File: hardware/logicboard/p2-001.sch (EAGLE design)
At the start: 65 parts, among them IC1 74LS06N, IC11 74LS153D, IC12 LTC485S, IC13 LTC485S, IC2 4066N, J1 MKR, J11 Qwiic, J12 Qwiic, J13 Qwiic, J14 Qwiic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

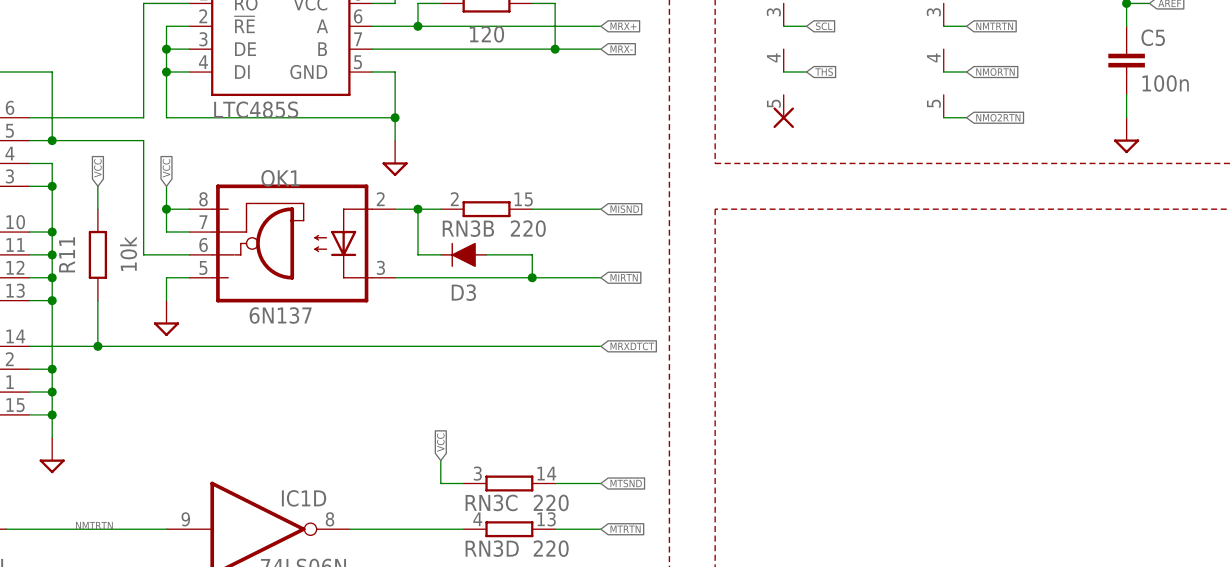
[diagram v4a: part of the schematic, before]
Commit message: TLP552 -> TLP2630.
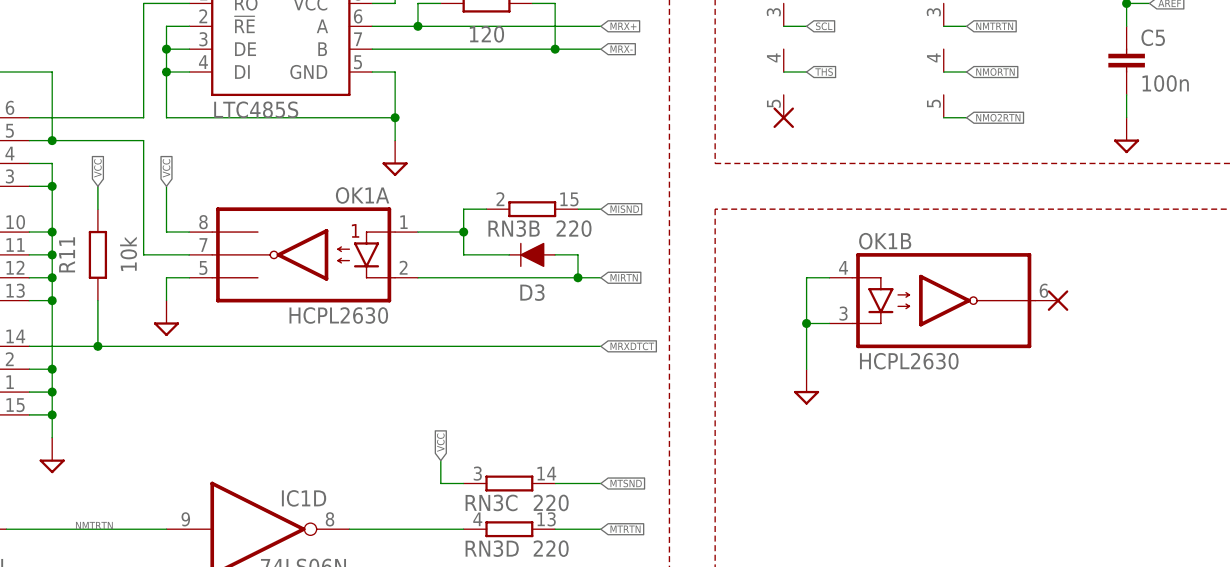
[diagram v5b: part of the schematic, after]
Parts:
- OK1: value 6N137 -> HCPL2630; device optocoupler:6N137 -> optocoupler:HCPL2630
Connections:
- net GND: now also OK1A.GND, OK1B.A2, OK1B.C2; no longer OK1.GND
- net MIDIINSND: now also OK1A.A1; no longer OK1.A
- net MIN: now also OK1A.VO1; no longer OK1.VO
- net MIRTN: now also OK1A.C1; no longer OK1.C
- net VCC: now also OK1A.VCC; no longer OK1.VCC, OK1.VE
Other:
- moved on the sheet: D3, RN3B
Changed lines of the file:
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@@
 <part name="MC1" library="adafruit" deviceset="ARDUINOMICRO" device=""/>
 <part name="SUPPLY18" library="supply2" deviceset="GND" device=""/>
-<part name="OK1" library="optocoupler" library_urn="urn:adsk.eagle:library:320" deviceset="6N137" device="" package3d_urn="urn:adsk.eagle:package:21941/1"/>
 <part name="D3" library="SparkFun-DiscreteSemi" library_urn="urn:adsk.eagle:library:514" deviceset="DIODE" device="-1N4148" package3d_urn="urn:adsk.eagle:package:38452/1" value=""/>
 <part name="LOGO1" library="SparkFun-Aesthetics" deviceset="OSHW-LOGO" device="S-COPPER" value="OSHW-LOGOS-COPPER"/>
@@
 <part name="RN4" library="resistor-net" library_urn="urn:adsk.eagle:library:343" deviceset="RN04" device="" package3d_urn="urn:adsk.eagle:package:24976/1" value="4.7k"/>
 <part name="X1" library="wirepad" library_urn="urn:adsk.eagle:library:412" deviceset="PAD-N" device=""/>
+<part name="OK1" library="optocoupler" library_urn="urn:adsk.eagle:library:320" deviceset="HCPL2630" device="" package3d_urn="urn:adsk.eagle:package:21941/1"/>
+<part name="SUPPLY1" library="supply2" deviceset="GND" device=""/>
+<part name="X2" library="wirepad" library_urn="urn:adsk.eagle:library:412" deviceset="PAD-N" device=""/>
 </parts>
 <sheets>
@@
 <instance part="MC1" gate="G$1" x="83.82" y="213.36" smashed="yes" rot="R270"/>
 <instance part="SUPPLY18" gate="GND" x="322.58" y="198.12" smashed="yes"/>
-<instance part="OK1" gate="A" x="177.8" y="119.38" smashed="yes" rot="MR0">
-<attribute name="NAME" x="177.8" y="127" size="1.778" layer="95" align="bottom-center"/>
-<attribute name="VALUE" x="177.8" y="111.76" size="1.778" layer="96" align="bottom-center"/>
-</instance>
-<instance part="D3" gate="G$1" x="198.12" y="119.38" smashed="yes" rot="R180">
-<attribute name="NAME" x="198.12" y="114.3" size="1.778" layer="95" align="bottom-center"/>
-<attribute name="VALUE" x="200.66" y="121.412" size="1.778" layer="96" font="vector" rot="R180" align="top-left"/>
+<instance part="D3" gate="G$1" x="205.74" y="119.38" smashed="yes" rot="R180">
+<attribute name="NAME" x="205.74" y="114.3" size="1.778" layer="95" align="bottom-center"/>
+<attribute name="VALUE" x="208.28" y="121.412" size="1.778" layer="96" font="vector" rot="R180" align="top-left"/>
 </instance>
 <instance part="LOGO1" gate="G$1" x="370.84" y="248.92" smashed="yes"/>
@@
 <attribute name="NAME" x="195.58" y="14.732" size="1.778" layer="95"/>
 </instance>
-<instance part="RN3" gate="B" x="200.66" y="124.46" smashed="yes">
-<attribute name="VALUE" x="203.2" y="121.412" size="1.778" layer="96"/>
-<attribute name="NAME" x="195.58" y="121.412" size="1.778" layer="95"/>
+<instance part="RN3" gate="B" x="205.74" y="124.46" smashed="yes">
+<attribute name="VALUE" x="208.28" y="121.412" size="1.778" layer="96"/>
+<attribute name="NAME" x="200.66" y="121.412" size="1.778" layer="95"/>
 </instance>
 <instance part="RN3" gate="C" x="203.2" y="93.98" smashed="yes">
@@
 </instance>
 <instance part="X1" gate="G$1" x="233.68" y="134.62" smashed="yes"/>
+<instance part="OK1" gate="A" x="180.34" y="119.38" smashed="yes" rot="MR0">
+<attribute name="NAME" x="189.865" y="125.095" size="1.778" layer="95" rot="MR0"/>
+<attribute name="VALUE" x="189.865" y="111.76" size="1.778" layer="96" rot="MR0"/>
+</instance>
+<instance part="OK1" gate="B" x="251.46" y="114.3" smashed="yes">
+<attribute name="NAME" x="241.935" y="120.015" size="1.778" layer="95"/>
+<attribute name="VALUE" x="241.935" y="106.68" size="1.778" layer="96"/>
+</instance>
+<instance part="SUPPLY1" gate="GND" x="236.22" y="104.14" smashed="yes"/>
+<instance part="X2" gate="G$1" x="264.16" y="114.3" smashed="yes"/>
 </instances>
 <busses>
@@
 </segment>
 <segment>
-<pinref part="OK1" gate="A" pin="GND"/>
 <pinref part="SUPPLY29" gate="GND" pin="GND"/>
 <wire x1="167.64" y1="116.84" x2="165.1" y2="116.84" width="0.1524" layer="91"/>
 <wire x1="165.1" y1="116.84" x2="165.1" y2="114.3" width="0.1524" layer="91"/>
+<pinref part="OK1" gate="A" pin="GND"/>
 </segment>
 <segment>
@@
 <label x="43.18" y="162.56" size="0.8128" layer="95" xref="yes"/>
 </segment>
+<segment>
+<pinref part="OK1" gate="B" pin="A2"/>
+<wire x1="238.76" y1="116.84" x2="236.22" y2="116.84" width="0.1524" layer="91"/>
+<pinref part="OK1" gate="B" pin="C2"/>
+<wire x1="238.76" y1="111.76" x2="236.22" y2="111.76" width="0.1524" layer="91"/>
+<wire x1="236.22" y1="111.76" x2="236.22" y2="116.84" width="0.1524" layer="91"/>
+<wire x1="236.22" y1="111.76" x2="236.22" y2="106.68" width="0.1524" layer="91"/>
+<junction x="236.22" y="111.76"/>
+<pinref part="SUPPLY1" gate="GND" pin="GND"/>
+</segment>
 </net>
 <net name="VCC" class="2">
@@
 </segment>
 <segment>
-<pinref part="OK1" gate="A" pin="VE"/>
 <wire x1="167.64" y1="121.92" x2="165.1" y2="121.92" width="0.1524" layer="91"/>
-<wire x1="165.1" y1="121.92" x2="165.1" y2="124.46" width="0.1524" layer="91"/>
+<wire x1="165.1" y1="121.92" x2="165.1" y2="127" width="0.1524" layer="91"/>
+<label x="165.1" y="127" size="0.8128" layer="95" rot="R90" xref="yes"/>
 <pinref part="OK1" gate="A" pin="VCC"/>
-<wire x1="165.1" y1="124.46" x2="165.1" y2="127" width="0.1524" layer="91"/>
-<wire x1="167.64" y1="124.46" x2="165.1" y2="124.46" width="0.1524" layer="91"/>
-<junction x="165.1" y="124.46"/>
-<label x="165.1" y="127" size="0.8128" layer="95" rot="R90" xref="yes"/>
 </segment>
 <segment>
@@
 <net name="MIDIINSND" class="0">
 <segment>
-<pinref part="OK1" gate="A" pin="A"/>
-<wire x1="193.04" y1="124.46" x2="190.5" y2="124.46" width="0.1524" layer="91"/>
-<wire x1="193.04" y1="124.46" x2="193.04" y2="119.38" width="0.1524" layer="91"/>
+<wire x1="198.12" y1="124.46" x2="198.12" y2="121.92" width="0.1524" layer="91"/>
 <pinref part="D3" gate="G$1" pin="C"/>
-<wire x1="193.04" y1="119.38" x2="195.58" y2="119.38" width="0.1524" layer="91"/>
-<wire x1="195.58" y1="124.46" x2="193.04" y2="124.46" width="0.1524" layer="91"/>
-<junction x="193.04" y="124.46"/>
+<wire x1="198.12" y1="121.92" x2="198.12" y2="119.38" width="0.1524" layer="91"/>
+<wire x1="198.12" y1="119.38" x2="203.2" y2="119.38" width="0.1524" layer="91"/>
+<wire x1="200.66" y1="124.46" x2="198.12" y2="124.46" width="0.1524" layer="91"/>
 <pinref part="RN3" gate="B" pin="1"/>
+<pinref part="OK1" gate="A" pin="A1"/>
+<wire x1="193.04" y1="121.92" x2="198.12" y2="121.92" width="0.1524" layer="91"/>
+<junction x="198.12" y="121.92"/>
 </segment>
 </net>
@@
 <segment>
 <pinref part="IC11" gate="A" pin="1C1"/>
-<pinref part="OK1" gate="A" pin="VO"/>
 <wire x1="149.86" y1="132.08" x2="152.4" y2="132.08" width="0.1524" layer="91"/>
 <wire x1="152.4" y1="132.08" x2="162.56" y2="132.08" width="0.1524" layer="91"/>
@@
 <wire x1="132.08" y1="144.78" x2="139.7" y2="144.78" width="0.1524" layer="91"/>
 <junction x="139.7" y="144.78"/>
+<pinref part="OK1" gate="A" pin="VO1"/>
 </segment>
 </net>
@@
 <net name="MISND" class="0">
 <segment>
-<wire x1="205.74" y1="124.46" x2="213.36" y2="124.46" width="0.1524" layer="91"/>
+<wire x1="210.82" y1="124.46" x2="213.36" y2="124.46" width="0.1524" layer="91"/>
 <label x="213.36" y="124.46" size="0.8128" layer="95" xref="yes"/>
 <pinref part="RN3" gate="B" pin="2"/>
@@
 <segment>
 <pinref part="D3" gate="G$1" pin="A"/>
-<wire x1="200.66" y1="119.38" x2="205.74" y2="119.38" width="0.1524" layer="91"/>
-<wire x1="205.74" y1="119.38" x2="205.74" y2="116.84" width="0.1524" layer="91"/>
-<pinref part="OK1" gate="A" pin="C"/>
-<wire x1="205.74" y1="116.84" x2="190.5" y2="116.84" width="0.1524" layer="91"/>
-<wire x1="205.74" y1="116.84" x2="213.36" y2="116.84" width="0.1524" layer="91"/>
-<junction x="205.74" y="116.84"/>
+<wire x1="208.28" y1="119.38" x2="210.82" y2="119.38" width="0.1524" layer="91"/>
+<wire x1="210.82" y1="119.38" x2="210.82" y2="116.84" width="0.1524" layer="91"/>
+<wire x1="210.82" y1="116.84" x2="193.04" y2="116.84" width="0.1524" layer="91"/>
+<wire x1="210.82" y1="116.84" x2="213.36" y2="116.84" width="0.1524" layer="91"/>
+<junction x="210.82" y="116.84"/>
 <label x="213.36" y="116.84" size="0.8128" layer="95" xref="yes"/>
-</segment>
-</net>
+<pinref part="OK1" gate="A" pin="C1"/>
+</segment>
+</net>

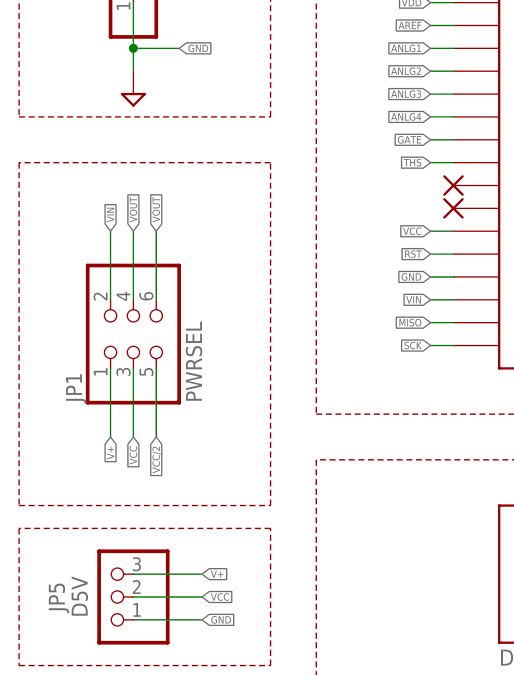
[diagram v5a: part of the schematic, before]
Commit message: Pads to close V+ and Vin.
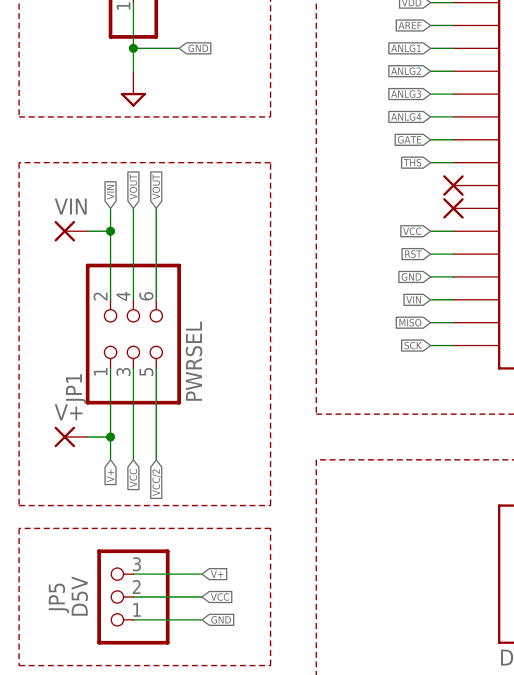
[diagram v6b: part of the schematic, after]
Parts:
- added V+, VIN: (no value), wirepad:SMD2
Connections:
- net V+: now also V+.P
- net VIN: now also VIN.P
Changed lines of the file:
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@@
 <part name="SUPPLY1" library="supply2" deviceset="GND" device=""/>
 <part name="X2" library="wirepad" library_urn="urn:adsk.eagle:library:412" deviceset="PAD-N" device=""/>
+<part name="V+" library="wirepad" library_urn="urn:adsk.eagle:library:412" deviceset="SMD2" device="" package3d_urn="urn:adsk.eagle:package:30839/1"/>
+<part name="VIN" library="wirepad" library_urn="urn:adsk.eagle:library:412" deviceset="SMD2" device="" package3d_urn="urn:adsk.eagle:package:30839/1"/>
 </parts>
 <sheets>
@@
 <instance part="SUPPLY1" gate="GND" x="236.22" y="104.14" smashed="yes"/>
 <instance part="X2" gate="G$1" x="264.16" y="114.3" smashed="yes"/>
+<instance part="V+" gate="1" x="27.94" y="182.88" smashed="yes">
+<attribute name="NAME" x="26.797" y="184.7342" size="1.778" layer="95"/>
+<attribute name="VALUE" x="26.797" y="179.578" size="1.778" layer="96"/>
+</instance>
+<instance part="VIN" gate="1" x="27.94" y="205.74" smashed="yes">
+<attribute name="NAME" x="26.797" y="207.5942" size="1.778" layer="95"/>
+<attribute name="VALUE" x="26.797" y="202.438" size="1.778" layer="96"/>
+</instance>
 </instances>
 <busses>
@@
 <segment>
 <pinref part="JP1" gate="A" pin="3"/>
-<wire x1="35.56" y1="190.5" x2="35.56" y2="182.88" width="0.1524" layer="91"/>
-<label x="35.56" y="182.88" size="0.8128" layer="95" rot="R270" xref="yes"/>
+<wire x1="35.56" y1="190.5" x2="35.56" y2="180.34" width="0.1524" layer="91"/>
+<label x="35.56" y="180.34" size="0.8128" layer="95" rot="R270" xref="yes"/>
 </segment>
 <segment>
@@
 <pinref part="JP1" gate="A" pin="2"/>
 <wire x1="33.02" y1="198.12" x2="33.02" y2="205.74" width="0.1524" layer="91"/>
-<label x="33.02" y="205.74" size="0.8128" layer="95" rot="R90" xref="yes"/>
+<label x="33.02" y="208.28" size="0.8128" layer="95" rot="R90" xref="yes"/>
+<wire x1="33.02" y1="205.74" x2="33.02" y2="208.28" width="0.1524" layer="91"/>
+<wire x1="33.02" y1="205.74" x2="30.48" y2="205.74" width="0.1524" layer="91"/>
+<junction x="33.02" y="205.74"/>
+<pinref part="VIN" gate="1" pin="P"/>
 </segment>
 </net>
@@
 <segment>
 <pinref part="JP1" gate="A" pin="5"/>
-<wire x1="38.1" y1="190.5" x2="38.1" y2="182.88" width="0.1524" layer="91"/>
-<label x="38.1" y="182.88" size="0.8128" layer="95" rot="R270" xref="yes"/>
+<wire x1="38.1" y1="190.5" x2="38.1" y2="180.34" width="0.1524" layer="91"/>
+<label x="38.1" y="180.34" size="0.8128" layer="95" rot="R270" xref="yes"/>
 </segment>
 <segment>
@@
 <segment>
 <pinref part="JP1" gate="A" pin="4"/>
-<wire x1="35.56" y1="198.12" x2="35.56" y2="205.74" width="0.1524" layer="91"/>
-<label x="35.56" y="205.74" size="0.8128" layer="95" rot="R90" xref="yes"/>
+<wire x1="35.56" y1="198.12" x2="35.56" y2="208.28" width="0.1524" layer="91"/>
+<label x="35.56" y="208.28" size="0.8128" layer="95" rot="R90" xref="yes"/>
 </segment>
 <segment>
 <pinref part="JP1" gate="A" pin="6"/>
-<wire x1="38.1" y1="198.12" x2="38.1" y2="205.74" width="0.1524" layer="91"/>
-<label x="38.1" y="205.74" size="0.8128" layer="95" rot="R90" xref="yes"/>
+<wire x1="38.1" y1="198.12" x2="38.1" y2="208.28" width="0.1524" layer="91"/>
+<label x="38.1" y="208.28" size="0.8128" layer="95" rot="R90" xref="yes"/>
 </segment>
 </net>
@@
 <pinref part="JP1" gate="A" pin="1"/>
 <wire x1="33.02" y1="190.5" x2="33.02" y2="182.88" width="0.1524" layer="91"/>
-<label x="33.02" y="182.88" size="0.8128" layer="95" rot="R270" xref="yes"/>
-</segment>
-<segment>
+<label x="33.02" y="180.34" size="0.8128" layer="95" rot="R270" xref="yes"/>
+<wire x1="33.02" y1="182.88" x2="33.02" y2="180.34" width="0.1524" layer="91"/>
+<wire x1="33.02" y1="182.88" x2="30.48" y2="182.88" width="0.1524" layer="91"/>
+<junction x="33.02" y="182.88"/>
+<pinref part="V+" gate="1" pin="P"/>
+</segment>
+<segment>

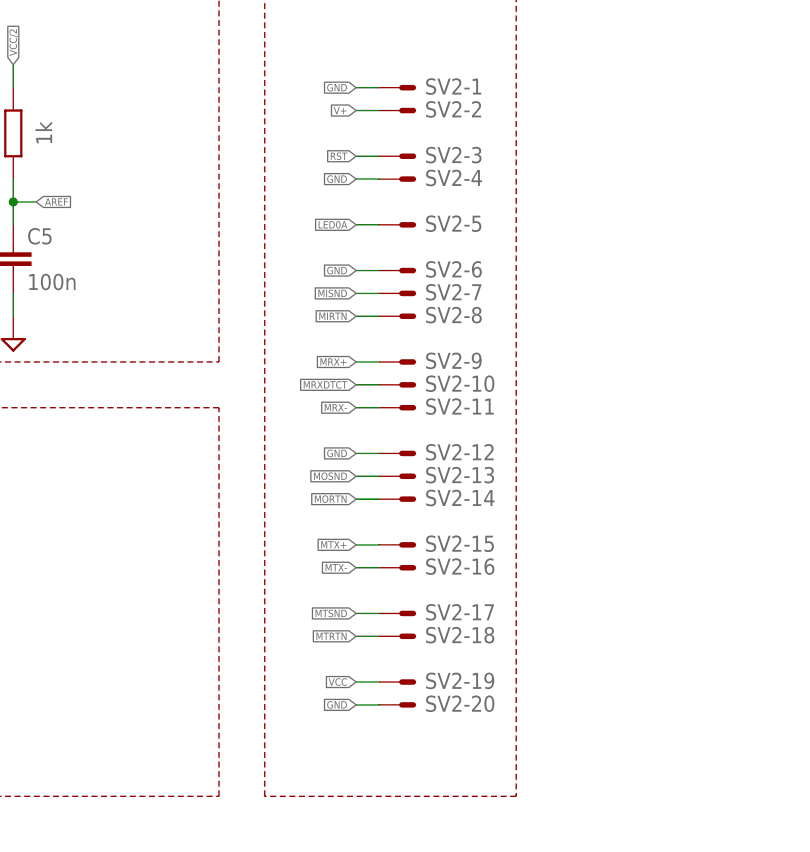
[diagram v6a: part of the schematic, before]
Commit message: Updated backside port to 2.0.
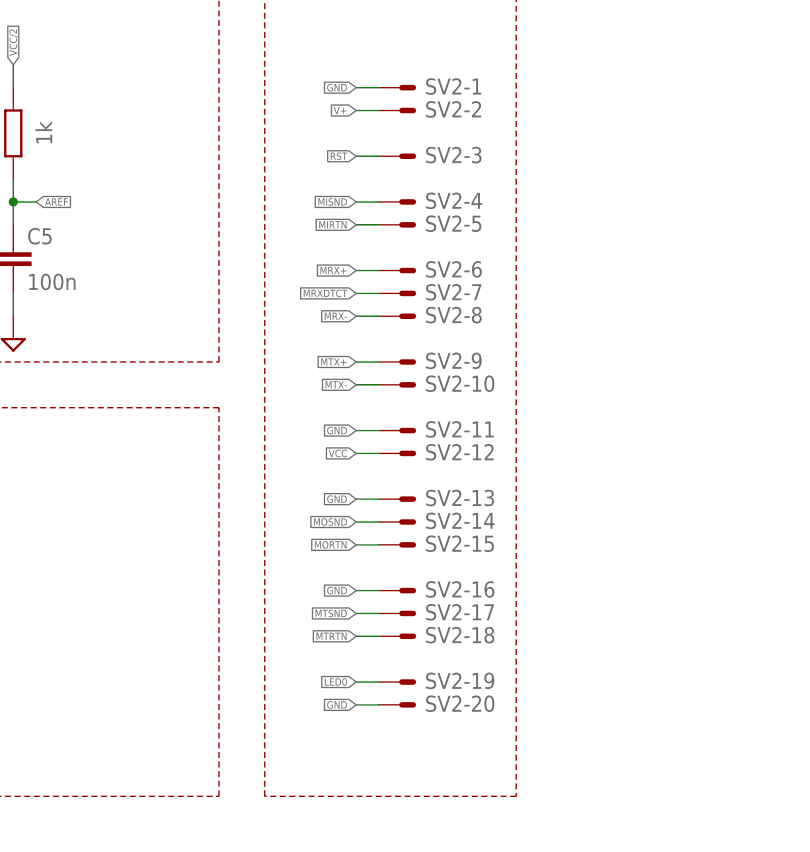
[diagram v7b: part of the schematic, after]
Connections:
- net GND: now also SV2-11.S, SV2-13.S, SV2-16.S; no longer SV2-12.S, SV2-4.S, SV2-6.S
- net LED0: now also SV2-19.S
- net LED0A: no longer SV2-5.S
- net MIRTN: now also SV2-5.S; no longer SV2-8.S
- net MISND: now also SV2-4.S; no longer SV2-7.S
- net MORTN: now also SV2-15.S; no longer SV2-14.S
- net MOSND: now also SV2-14.S; no longer SV2-13.S
- net MRX+: now also SV2-6.S; no longer SV2-9.S
- net MRX-: now also SV2-8.S; no longer SV2-11.S
- net MRXDTCT: now also SV2-7.S; no longer SV2-10.S
- net MTX+: now also SV2-9.S; no longer SV2-15.S
- net MTX-: now also SV2-10.S; no longer SV2-16.S
- net VCC: now also SV2-12.S; no longer SV2-19.S
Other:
- moved on the sheet: SV2-11, SV2-13, SV2-14, SV2-16, SV2-4

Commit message: Hotfix of the original P2.
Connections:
- net MIN: now also RN1.2
- net RX: no longer RN1.2
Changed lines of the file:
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@@
-</segment>
-<segment>
-<pinref part="RN1" gate="1" pin="2"/>
-<wire x1="251.46" y1="149.86" x2="254" y2="149.86" width="0.1524" layer="91"/>
-<label x="254" y="149.86" size="0.8128" layer="95" xref="yes"/>
 </segment>
 <segment>
@@
 <pinref part="OK1" gate="A" pin="VO1"/>
 </segment>
-</net>
+<segment>
+<pinref part="RN1" gate="1" pin="2"/>
+<wire x1="251.46" y1="149.86" x2="254" y2="149.86" width="0.1524" layer="91"/>
+<label x="254" y="149.86" size="0.8128" layer="95" xref="yes"/>
+</segment>
+</net>
